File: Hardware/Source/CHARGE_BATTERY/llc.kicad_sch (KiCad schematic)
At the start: 11 parts, among them M1 650 V, 24 A, M2 650 V, 24 A

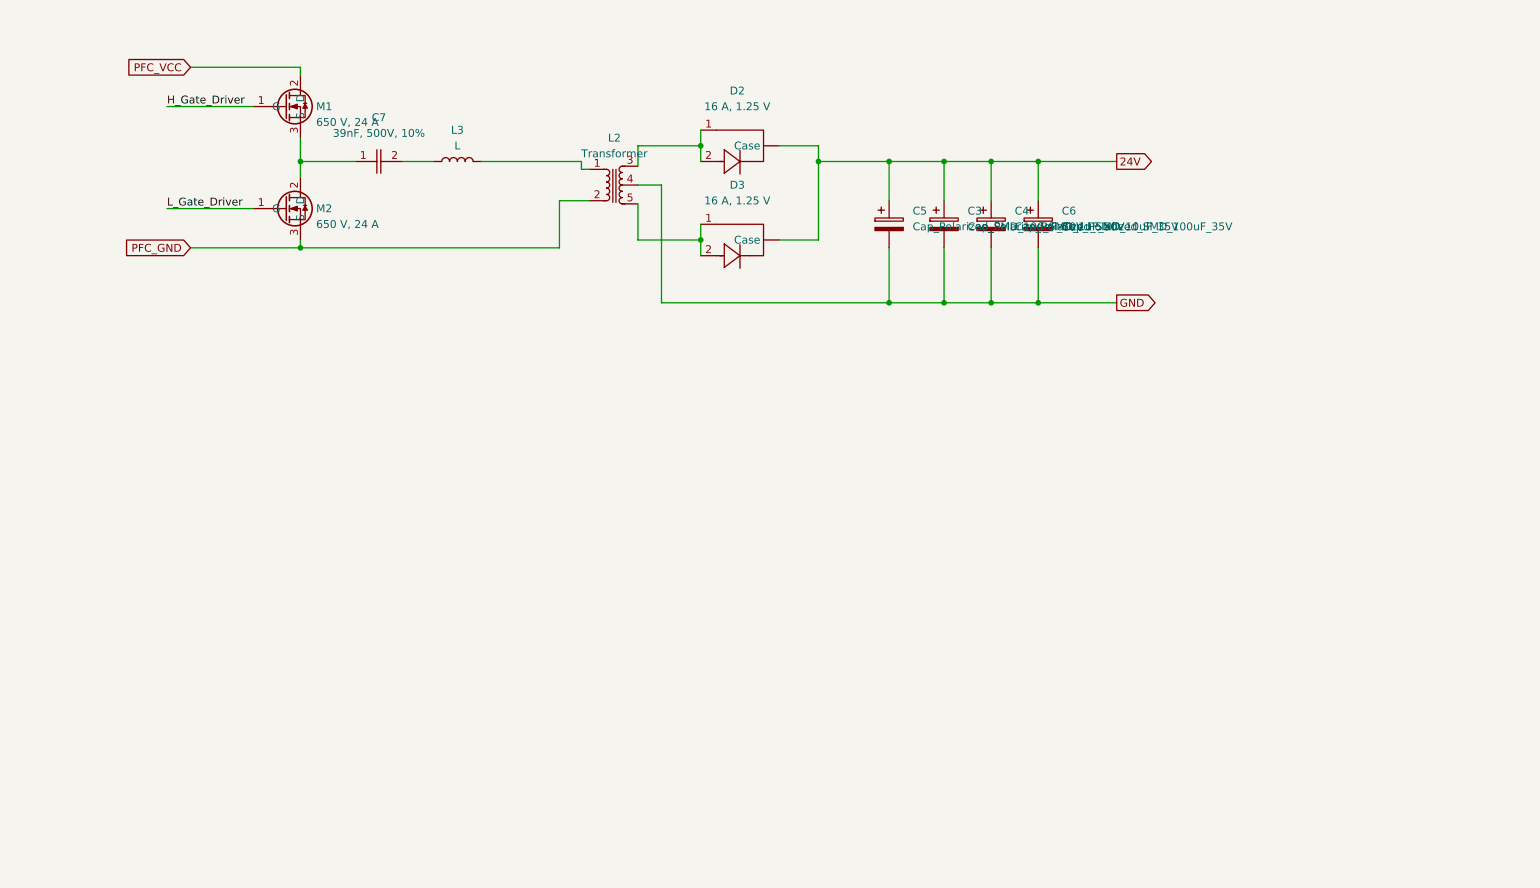
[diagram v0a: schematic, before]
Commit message: Add MCU Schematic, missing library components for MCU, not done
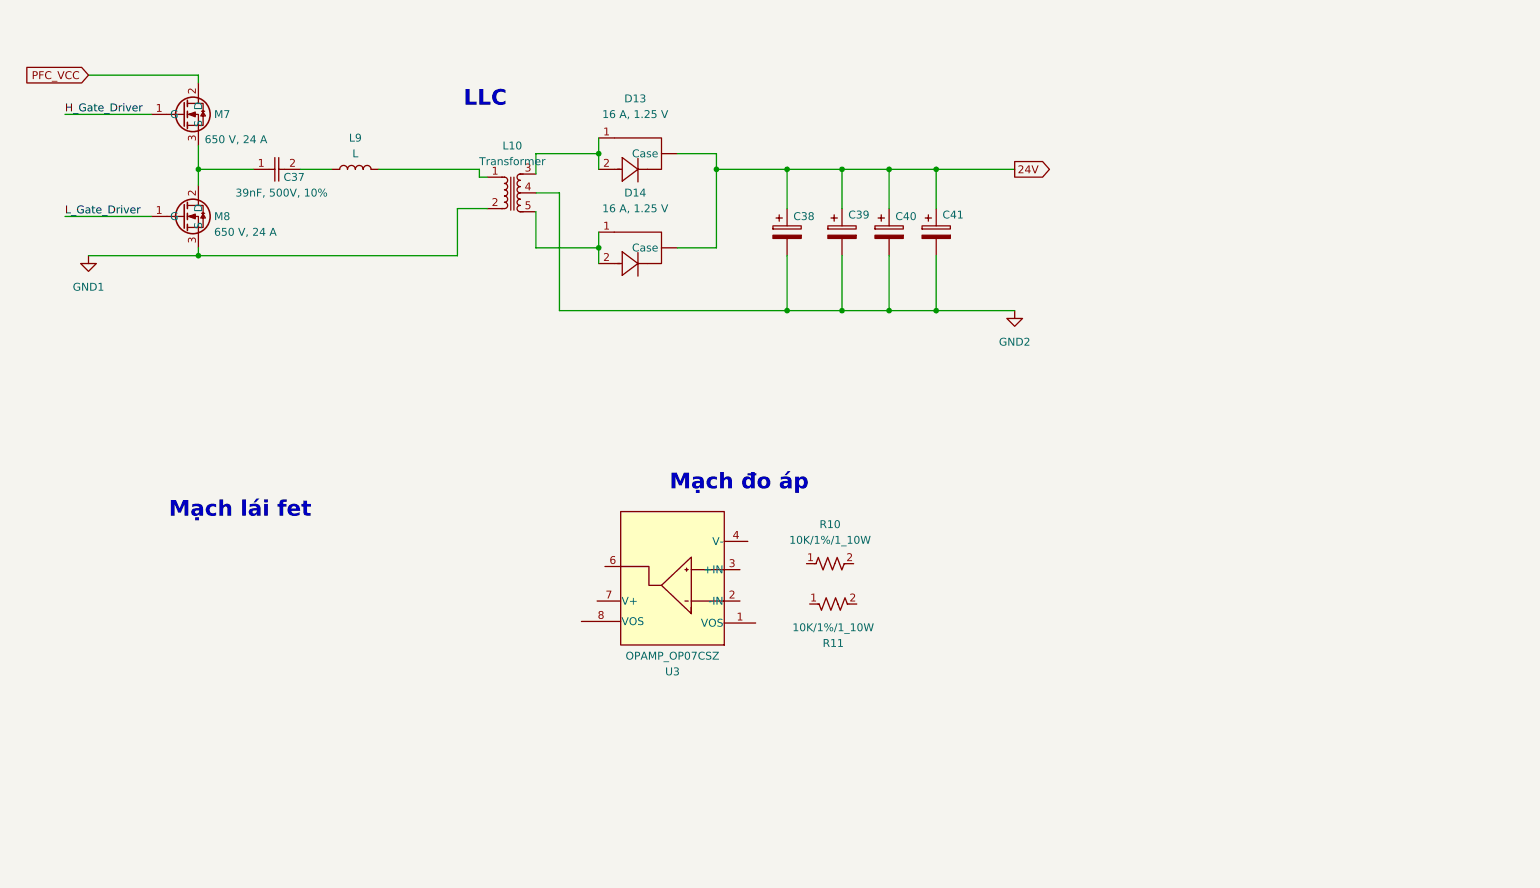
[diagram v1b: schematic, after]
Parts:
- removed C3: Cap_Polarized_SMD_1uF_50V, charge_battery_footprint_lib:Cap_Polarized_SMD_1uF_50V, symbol charge_battery_sym_lib:Cap_Polarized_SMD_1uF_50V
- removed C4: Cap_Polarized_SMD_10uF_35V, charge_battery_footprint_lib:Cap_Polarized_SMD_10uF_35V, symbol charge_battery_sym_lib:Cap_Polarized_SMD_10uF_35V
- removed C5: Cap_Polarized_SMD_100nF_50V, charge_battery_footprint_lib:Cap_Polarized_SMD_100nF (0.1uF) 50V, symbol charge_battery_sym_lib:Cap_Polarized_SMD_100nF (0.1uF) 50V
- removed C6: Cap_Polarized_SMD_100uF_35V, charge_battery_footprint_lib:Cap_Polarized_SMD_100uF_35V, symbol charge_battery_sym_lib:Cap_Polarized_SMD_100uF_35V
- removed C7: 39nF, 500V, 10%, charge_battery_footprint_lib:Ceramic_Cap_0.039uF_500V_1210, symbol charge_battery_sym_lib:Ceramic_Cap_SMD_0.039uF_500V_10%
- removed D2, D3: 16 A, 1.25 V, charge_battery_footprint_lib:Diode_Schottky_IDH06G65C6, symbol charge_battery_sym_lib: Diode_Schottky_IDH06G65C6
- removed L2: Transformer, charge_battery_footprint_lib:Transformer, symbol charge_battery_sym_lib:Transformer
- removed L3: L, Inductor_SMD:L_6.3x6.3_H3, symbol Device:L
- removed M1, M2: 650 V, 24 A, charge_battery_footprint_lib:IPP65R095C7, symbol charge_battery_sym_lib:IPP65R095C7
- added C37: 39nF, 500V, 10%, charge_battery_footprint_lib:Ceramic_Cap_0.039uF_500V_1210, symbol charge_battery_sym_lib:Ceramic_Cap_SMD_0.039uF_500V_10%
- added C38: Cap_Polarized_SMD_100nF_50V, charge_battery_footprint_lib:Cap_Polarized_SMD_100nF (0.1uF) 50V, symbol charge_battery_sym_lib:Cap_Polarized_SMD_100nF (0.1uF) 50V
- added C39: Cap_Polarized_SMD_1uF_50V, charge_battery_footprint_lib:Cap_Polarized_SMD_1uF_50V, symbol charge_battery_sym_lib:Cap_Polarized_SMD_1uF_50V
- added C40: Cap_Polarized_SMD_10uF_35V, charge_battery_footprint_lib:Cap_Polarized_SMD_10uF_35V, symbol charge_battery_sym_lib:Cap_Polarized_SMD_10uF_35V
- added C41: Cap_Polarized_SMD_100uF_35V, charge_battery_footprint_lib:Cap_Polarized_SMD_100uF_35V, symbol charge_battery_sym_lib:Cap_Polarized_SMD_100uF_35V
- added D13, D14: 16 A, 1.25 V, charge_battery_footprint_lib:Diode_Schottky_IDH06G65C6, symbol charge_battery_sym_lib: Diode_Schottky_IDH06G65C6
- added L10: Transformer, charge_battery_footprint_lib:Transformer, symbol charge_battery_sym_lib:Transformer
- added L9: L, Inductor_SMD:L_6.3x6.3_H3, symbol Device:L
- added M7, M8: 650 V, 24 A, charge_battery_footprint_lib:IPP65R095C7, symbol charge_battery_sym_lib:IPP65R095C7
- added R10, R11: 10K/1%/1_10W, charge_battery_footprint_lib:Res_10K_0603, symbol charge_battery_sym_lib:Res_10K_0603_1%
- added U3: OPAMP_OP07CSZ, charge_battery_footprint_lib:OPAMP_OP07CSZ, symbol charge_battery_sym_lib:OPAMP_OP07CSZ
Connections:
- net 24V: now also C38.1, C39.1, C40.1, C41.1, D13. (Case), D14. (Case)
- net H_Gate_Driver: now also M7.1 (G)
- net L_Gate_Driver: now also M8.1 (G)
- net PFC_VCC: now also M7.2 (D)
- new net: D13.1, D13.2, L10.3
- new net: L10.1, L9.2
- new net: D14.1, D14.2, L10.5
- new net: C37.2, L9.1
- new net: C37.1, M7.3 (S), M8.2 (D)
- new net GND1: L10.2, M8.3 (S)
- new net GND2: C38.2, C39.2, C40.2, C41.2, L10.4
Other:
- note added: "LLC"
- note added: "Mạch lái fet"
- note added: "Mạch đo áp"
- title: (none) -> LLC Circuit

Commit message: Combine Sche in Source: PFC, LLC, F1, F4, ESP32
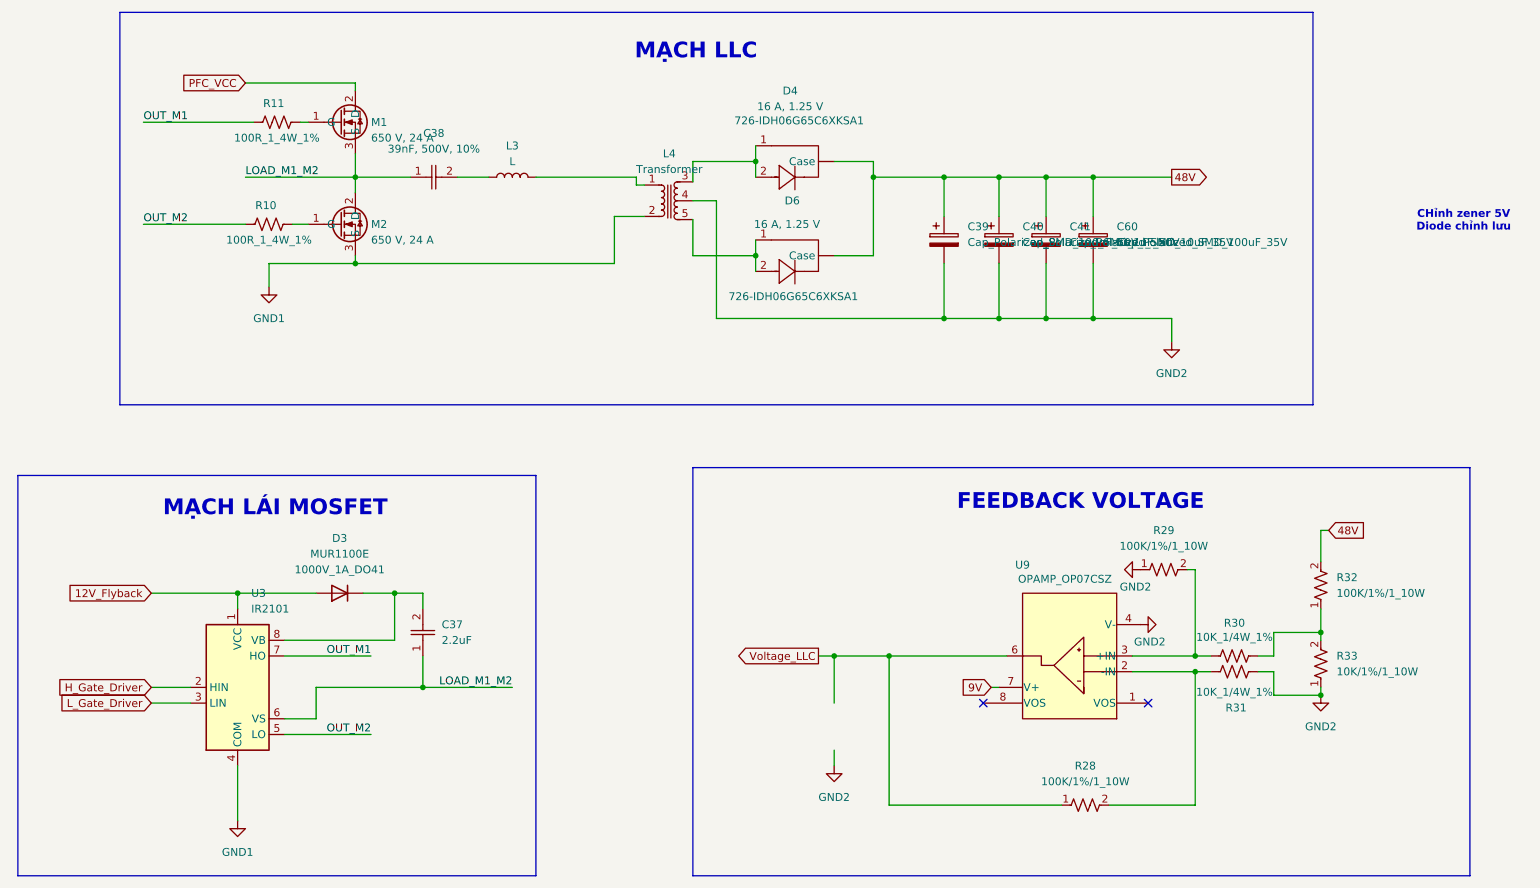
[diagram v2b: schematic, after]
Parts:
- removed C37: 39nF, 500V, 10%, charge_battery_footprint_lib:Ceramic_Cap_0.039uF_500V_1210, symbol charge_battery_sym_lib:Ceramic_Cap_SMD_0.039uF_500V_10%
- removed C38: Cap_Polarized_SMD_100nF_50V, charge_battery_footprint_lib:Cap_Polarized_SMD_100nF (0.1uF) 50V, symbol charge_battery_sym_lib:Cap_Polarized_SMD_100nF (0.1uF) 50V
- removed C39: Cap_Polarized_SMD_1uF_50V, charge_battery_footprint_lib:Cap_Polarized_SMD_1uF_50V, symbol charge_battery_sym_lib:Cap_Polarized_SMD_1uF_50V
- removed C40: Cap_Polarized_SMD_10uF_35V, charge_battery_footprint_lib:Cap_Polarized_SMD_10uF_35V, symbol charge_battery_sym_lib:Cap_Polarized_SMD_10uF_35V
- removed C41: Cap_Polarized_SMD_100uF_35V, charge_battery_footprint_lib:Cap_Polarized_SMD_100uF_35V, symbol charge_battery_sym_lib:Cap_Polarized_SMD_100uF_35V
- removed D13, D14: 16 A, 1.25 V, charge_battery_footprint_lib:Diode_Schottky_IDH06G65C6, symbol charge_battery_sym_lib: Diode_Schottky_IDH06G65C6
- removed L10: Transformer, charge_battery_footprint_lib:Transformer, symbol charge_battery_sym_lib:Transformer
- removed L9: L, Inductor_SMD:L_6.3x6.3_H3, symbol Device:L
- removed M7, M8: 650 V, 24 A, charge_battery_footprint_lib:IPP65R095C7, symbol charge_battery_sym_lib:IPP65R095C7
- removed R10, R11: 10K/1%/1_10W, charge_battery_footprint_lib:Res_10K_0603, symbol charge_battery_sym_lib:Res_10K_0603_1%
- removed U3: OPAMP_OP07CSZ, charge_battery_footprint_lib:OPAMP_OP07CSZ, symbol charge_battery_sym_lib:OPAMP_OP07CSZ
- added C37: 2.2uF, Capacitor_SMD:C_0805_2012Metric_Pad1.18x1.45mm_HandSolder, symbol charge_battery_sym_lib:Ceramic_Cap_Hole_1uF_50V_
- added C38: 39nF, 500V, 10%, charge_battery_footprint_lib:Ceramic_Cap_0.039uF_500V_1210, symbol charge_battery_sym_lib:Ceramic_Cap_SMD_0.039uF_500V_10%
- added C39: Cap_Polarized_SMD_100nF_50V, charge_battery_footprint_lib:Cap_Polarized_SMD_100nF (0.1uF) 50V, symbol charge_battery_sym_lib:Cap_Polarized_SMD_100nF (0.1uF) 50V
- added C40: Cap_Polarized_SMD_1uF_50V, charge_battery_footprint_lib:Cap_Polarized_SMD_1uF_50V, symbol charge_battery_sym_lib:Cap_Polarized_SMD_1uF_50V
- added C41: Cap_Polarized_SMD_10uF_35V, charge_battery_footprint_lib:Cap_Polarized_SMD_10uF_35V, symbol charge_battery_sym_lib:Cap_Polarized_SMD_10uF_35V
- added C60: Cap_Polarized_SMD_100uF_35V, charge_battery_footprint_lib:Cap_Polarized_SMD_100uF_35V, symbol charge_battery_sym_lib:Cap_Polarized_SMD_100uF_35V
- added D3: MUR1100E, Diode_THT:D_DO-41_SOD81_P10.16mm_Horizontal, symbol Diode:UF5401
- added D4, D6: 16 A, 1.25 V, charge_battery_footprint_lib:Diode_Schottky_IDH06G65C6, symbol charge_battery_sym_lib: Diode_Schottky_IDH06G65C6
- added L3: L, Inductor_SMD:L_6.3x6.3_H3, symbol Device:L
- added L4: Transformer, charge_battery_footprint_lib:Transformer, symbol charge_battery_sym_lib:Transformer
- added M1, M2: 650 V, 24 A, charge_battery_footprint_lib:IPP65R095C7, symbol charge_battery_sym_lib:IPP65R095C7
- added R10, R11: 100R_1_4W_1%, charge_battery_footprint_lib:Res_220R_1_4W_1%, symbol charge_battery_sym_lib:Res_hole_220R_1/4W_1%
- added R28, R29, R32: 100K/1%/1_10W, charge_battery_footprint_lib:Res_200K_0603, symbol charge_battery_sym_lib:Res_200K_0603_1%
- added R30, R31: 10K_1/4W_1%, charge_battery_footprint_lib:Res_10K_1_4W_1%, symbol charge_battery_sym_lib:Res_hole_10K_1/4W_1%
- added R33: 10K/1%/1_10W, charge_battery_footprint_lib:Res_10K_0603, symbol charge_battery_sym_lib:Res_10K_0603_1%
- added U3: IR2101, charge_battery_footprint_lib:IR2101, symbol charge_battery_sym_lib:IR2101
- added U9: OPAMP_OP07CSZ, charge_battery_footprint_lib:OPAMP_OP07CSZ, symbol charge_battery_sym_lib:OPAMP_OP07CSZ
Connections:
- net GND1: now also L4.2, M2.3 (S), U3.4 (COM)
- net GND2: now also C39.2, C40.2, C41.2, C60.2, L4.4, R29.1, R31.2, R33.1, U9.4 (V-)
- net H_Gate_Driver: now also U3.2 (HIN)
- net L_Gate_Driver: now also U3.3 (LIN)
- net PFC_VCC: now also M1.2 (D)
- new net: C37.2, D3.1 (K), U3.8 (VB)
- new net: L3.2, L4.1
- new net: D4.1, D4.2, L4.3
- new net: D6.1, D6.2, L4.5
- new net: C38.2, L3.1
- new net: M1.1 (G), R11.2
- new net: R30.2, R32.1, R33.2
- new net: R28.2, R31.1, U9.2 (-IN)
- new net: M2.1 (G), R10.2
- new net: R29.2, R30.1, U9.3 (+IN)
- new net 12V_Flyback: D3.2 (A), U3.1 (VCC)
- new net 48V: C39.1, C40.1, C41.1, C60.1, D4. (Case), D6. (Case), R32.2
- new net 9V: U9.7 (V+)
- new net LOAD_M1_M2: C37.1, C38.1, M1.3 (S), M2.2 (D), U3.6 (VS)
- new net OUT_M1: R11.1, U3.7 (HO)
- new net OUT_M2: R10.1, U3.5 (LO)
- new net Voltage_LLC: R28.1, U9.6
- no-connect marks 0 -> 2
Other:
- note added: "CHỉnh zener 5V Diode chỉnh lưu"
- note added: "FEEDBACK VOLTAGE"
- note added: "MẠCH LLC"
- note added: "MẠCH LÁI MOSFET"
- note removed: "LLC"
- note removed: "Mạch lái fet"
- note removed: "Mạch đo áp"

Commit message: Merge branch 'dev_hardware' of https://github.com/DONGKHOA/CHARGE_BATTERY into dev_hardware
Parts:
- removed D4, D6: 16 A, 1.25 V, charge_battery_footprint_lib:Diode_Schottky_IDH06G65C6, symbol charge_battery_sym_lib: Diode_Schottky_IDH06G65C6
- added D4, D9: 16 A, 650 V, charge_battery_footprint_lib:Diode_Schottky_IDH06G65C6, symbol charge_battery_sym_lib:Diode_Schottky_IDH06G65C6
- added D6: BZV55B5V1, Diode_SMD:D_MiniMELF, symbol Diode:BZV55B5V1
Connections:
- net 48V: now also D4.2 (A), D9.2 (A)
- net GND2: now also D6.2 (A)
- net Voltage_LLC: now also D6.1 (K)
- net at L4.3: now also D9.1 (K)
- net at L4.5: now also D4.1 (K)
- net 12V_Flyback renamed +12V
- net 9V renamed +9V
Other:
- note removed: "CHỉnh zener 5V Diode chỉnh lưu"
- moved on the sheet: L3

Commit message: Update: Feedback Voltage
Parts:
- R32: value 100K/1%/1_10W -> 200K/1%/1_10W
- R33: value 10K/1%/1_10W -> 1.5K/1%/1_10W
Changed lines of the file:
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@@
 			)
 		)
-		(property "Value" "10K/1%/1_10W"
+		(property "Value" "1.5K/1%/1_10W"
 			(at 240.03 125.7299 90)
 			(effects
@@
 			)
 		)
-		(property "Value" "100K/1%/1_10W"
+		(property "Value" "200K/1%/1_10W"
 			(at 240.03 113.0299 90)
 			(effects
